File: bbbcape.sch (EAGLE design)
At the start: 13 parts

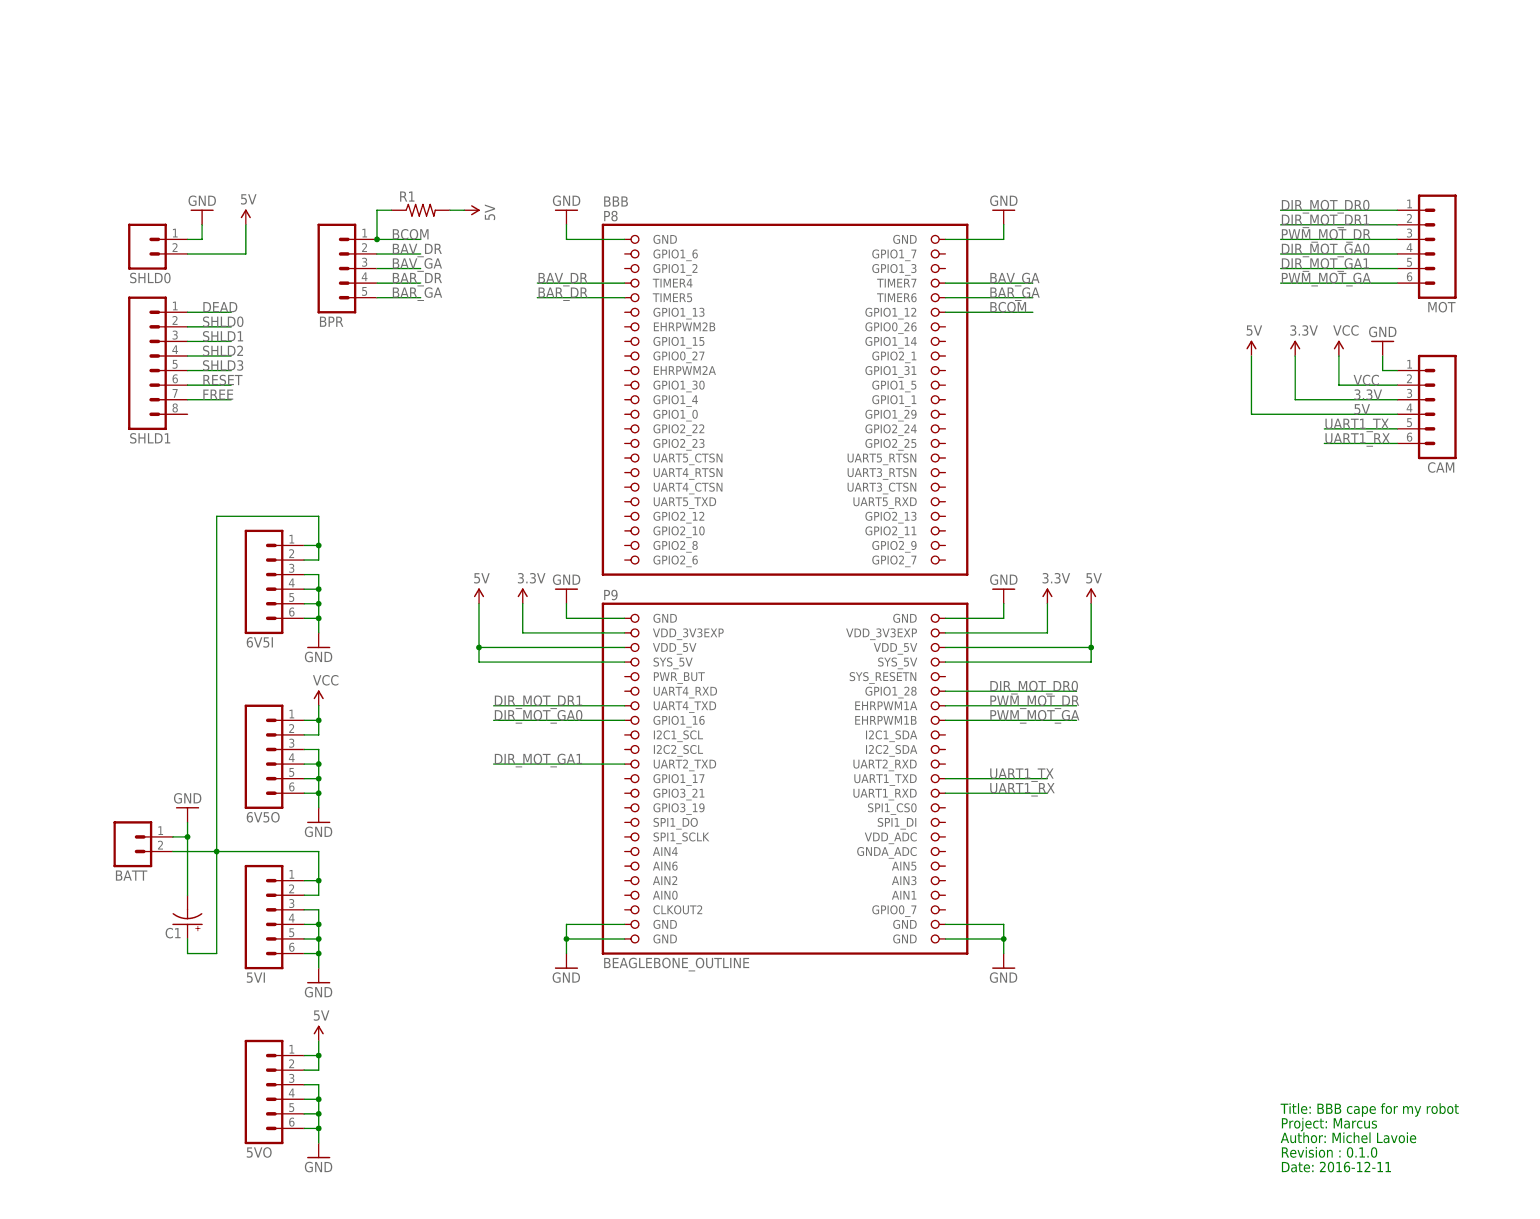
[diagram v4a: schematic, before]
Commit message: Connected GP2D12 rangefinders.
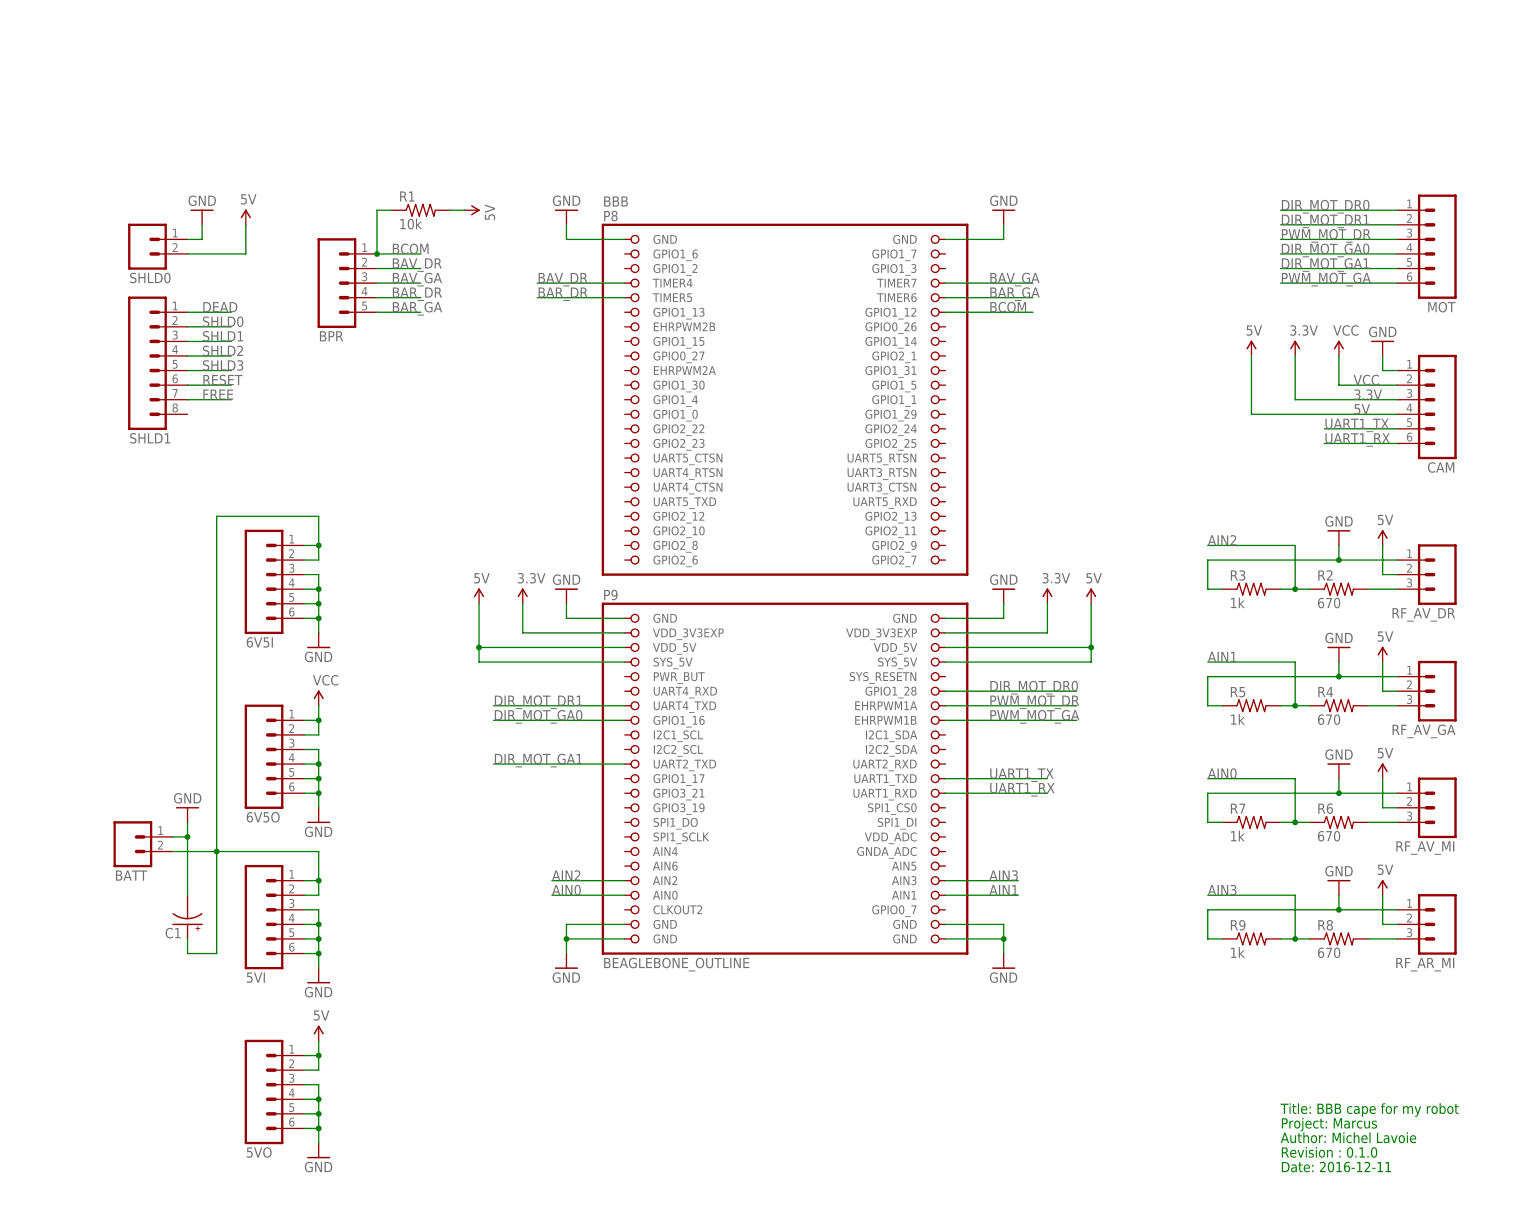
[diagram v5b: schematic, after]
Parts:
- added R2, R4, R6, R8: 670, SparkFun-Passives:RESISTORAXIAL-0.3
- added R3, R5, R7, R9: 1k, SparkFun-Passives:RESISTORAXIAL-0.3
- added RF_AR_MI, RF_AV_DR, RF_AV_GA, RF_AV_MI: (no value), SparkFun-Connectors:M03PTH
- R1: value (none) -> 10k
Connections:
- new net AIN0: BBB.AIN0, R6.1, R7.2
- new net AIN1: BBB.AIN1, R4.1, R5.2
- new net AIN2: BBB.AIN2, R2.1, R3.2
- new net AIN3: BBB.AIN3, R8.1, R9.2
- new net N$2: R2.2, RF_AV_DR.3
- new net N$4: R4.2
- new net N$5: R6.2
- new net N$6: R8.2
- net 5V: now also RF_AV_DR.2
- net GND: now also R3.1, R5.1, R7.1, R9.1, RF_AV_DR.1
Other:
- moved on the sheet: BPR

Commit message: Connected shields.
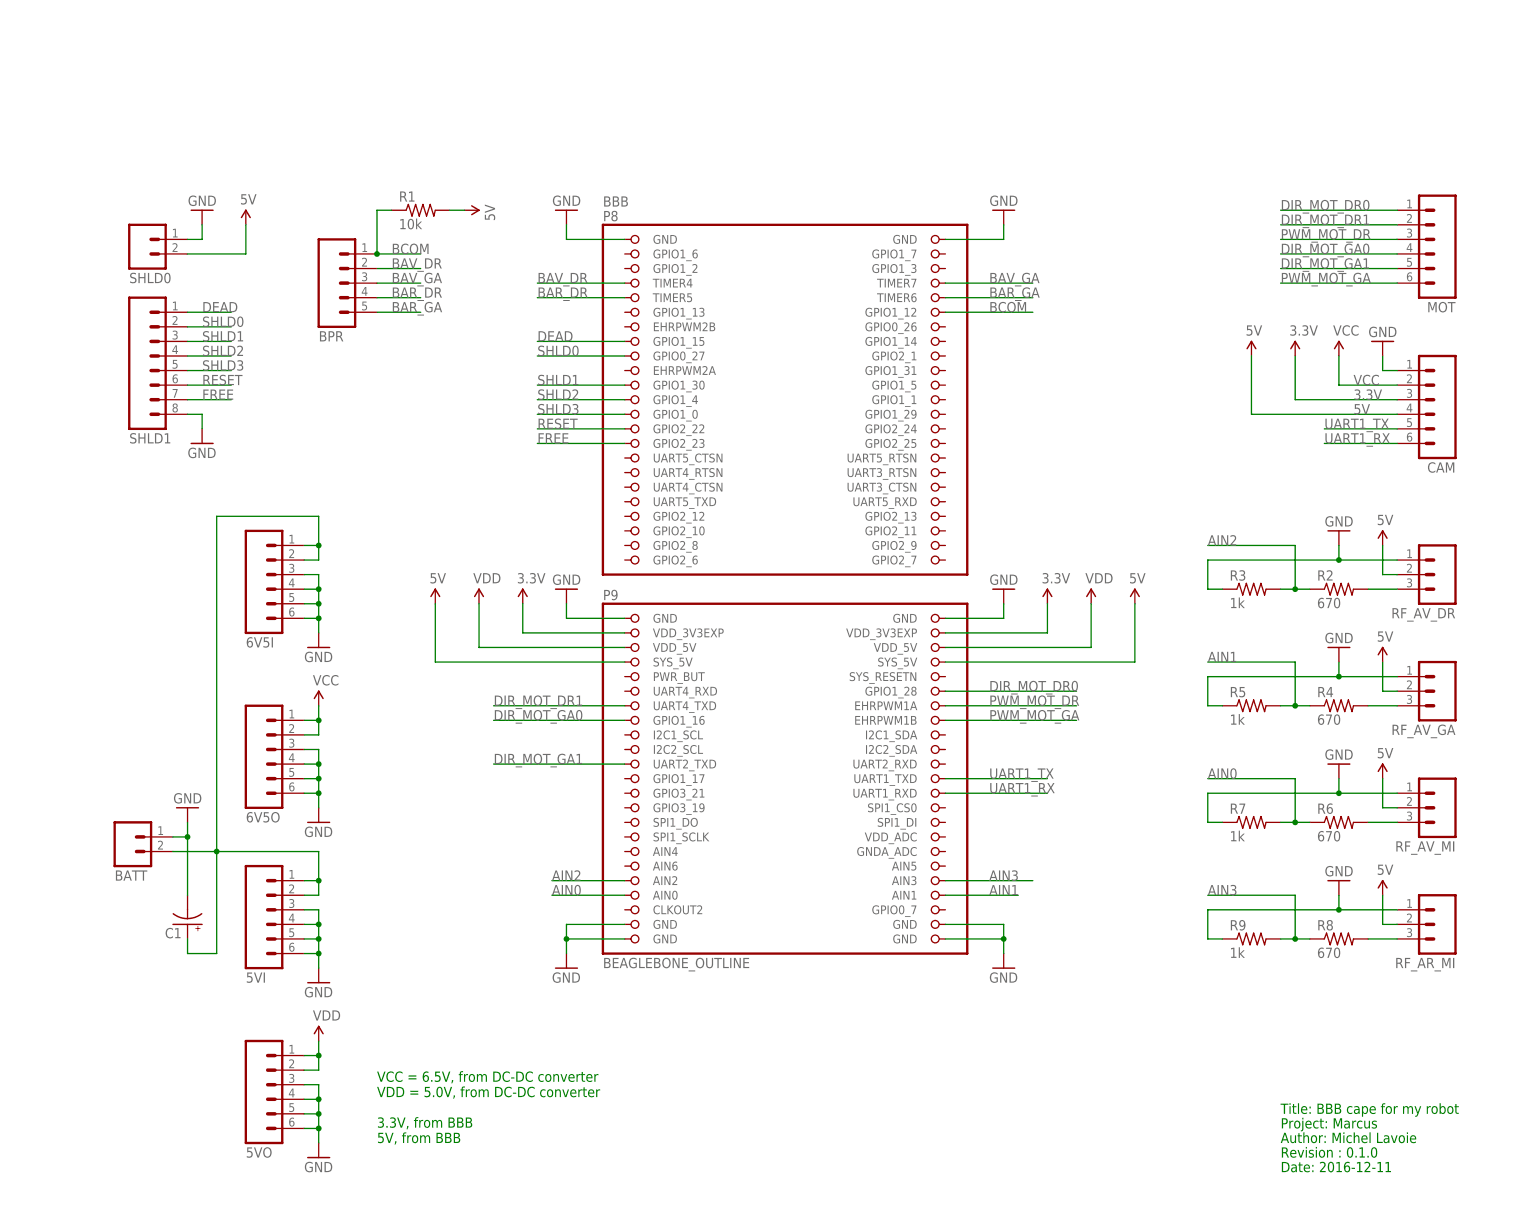
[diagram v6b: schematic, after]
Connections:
- new net VDD: 5VO.1, 5VO.2, BBB.VDD_5V@1, BBB.VDD_5V@2
- net 5V: no longer 5VO.1, 5VO.2, BBB.VDD_5V@1, BBB.VDD_5V@2
- net DEAD: now also BBB.GPIO1_15
- net FREE: now also BBB.GPIO2_23
- net GND: now also SHLD1.8
- net RESET: now also BBB.GPIO2_22
- net SHLD0: now also BBB.GPIO0_27
- net SHLD1: now also BBB.GPIO1_30
- net SHLD2: now also BBB.GPIO1_4
- net SHLD3: now also BBB.GPIO1_0
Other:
- note added: "VCC = 6.5V, from DC-DC converter VDD = 5.0V, from DC-DC converter 3.3V, from BBB 5V, from BBB"
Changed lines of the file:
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@@
 <setting verticaltext="up"/>
 </settings>
-<grid distance="0.1" unitdist="inch" unit="inch" style="lines" multiple="1" display="no" altdistance="0.01" altunitdist="inch" altunit="inch"/>
+<grid distance="0.1" unitdist="inch" unit="inch" style="dots" multiple="1" display="yes" altdistance="0.01" altunitdist="inch" altunit="inch"/>
 <layers>
 <layer number="1" name="Top" color="4" fill="1" visible="no" active="no"/>
@@
 <part name="GND6" library="SparkFun-Aesthetics" deviceset="GND" device=""/>
 <part name="GND7" library="SparkFun-Aesthetics" deviceset="GND" device=""/>
-<part name="SUPPLY1" library="SparkFun-Aesthetics" deviceset="5V" device=""/>
 <part name="BATT" library="SparkFun-Connectors" deviceset="M02" device="PTH"/>
 <part name="GND8" library="SparkFun-Aesthetics" deviceset="GND" device=""/>
@@
 <part name="GND17" library="SparkFun-Aesthetics" deviceset="GND" device=""/>
 <part name="SUPPLY13" library="SparkFun-Aesthetics" deviceset="5V" device=""/>
+<part name="SUPPLY14" library="SparkFun-Aesthetics" deviceset="VDD" device=""/>
+<part name="SUPPLY1" library="SparkFun-Aesthetics" deviceset="VDD" device=""/>
+<part name="SUPPLY15" library="SparkFun-Aesthetics" deviceset="VDD" device=""/>
+<part name="GND18" library="SparkFun-Aesthetics" deviceset="GND" device=""/>
 </parts>
 <sheets>
@@
 <text x="210.82" y="10.16" size="1.778" layer="91">Revision : 0.1.0</text>
 <text x="210.82" y="7.62" size="1.778" layer="91">Date: 2016-12-11</text>
+<text x="53.34" y="12.7" size="1.778" layer="91">VCC = 6.5V, from DC-DC converter
+VDD = 5.0V, from DC-DC converter
+3.3V, from BBB
+5V, from BBB</text>
 </plain>
 <instances>
@@
 <instance part="GND6" gate="1" x="86.36" y="43.18"/>
 <instance part="GND7" gate="1" x="162.56" y="43.18"/>
-<instance part="SUPPLY1" gate="G$1" x="43.18" y="30.48"/>
 <instance part="BATT" gate="G$1" x="10.16" y="66.04" rot="MR180"/>
 <instance part="GND8" gate="1" x="20.32" y="71.12" rot="R180"/>
@@
 <instance part="R1" gate="G$1" x="60.96" y="175.26"/>
 <instance part="SUPPLY3" gate="G$1" x="68.58" y="175.26" rot="R270"/>
-<instance part="SUPPLY4" gate="G$1" x="71.12" y="106.68"/>
-<instance part="SUPPLY5" gate="G$1" x="177.8" y="106.68"/>
+<instance part="SUPPLY4" gate="G$1" x="63.5" y="106.68"/>
+<instance part="SUPPLY5" gate="G$1" x="185.42" y="106.68"/>
 <instance part="SUPPLY6" gate="G$1" x="78.74" y="106.68"/>
 <instance part="SUPPLY7" gate="G$1" x="170.18" y="106.68"/>
@@
 <instance part="GND17" gate="1" x="220.98" y="58.42" rot="R180"/>
 <instance part="SUPPLY13" gate="G$1" x="228.6" y="55.88"/>
+<instance part="SUPPLY14" gate="VDD" x="71.12" y="106.68"/>
+<instance part="SUPPLY1" gate="VDD" x="43.18" y="30.48"/>
+<instance part="SUPPLY15" gate="VDD" x="177.8" y="106.68"/>
+<instance part="GND18" gate="1" x="22.86" y="134.62"/>
 </instances>
 <busses>
@@
 <wire x1="220.98" y1="53.34" x2="231.14" y2="53.34" width="0.1524" layer="91"/>
 <junction x="220.98" y="53.34"/>
+</segment>
+<segment>
+<pinref part="SHLD1" gate="G$1" pin="8"/>
+<wire x1="20.32" y1="139.7" x2="22.86" y2="139.7" width="0.1524" layer="91"/>
+<pinref part="GND18" gate="1" pin="GND"/>
+<wire x1="22.86" y1="139.7" x2="22.86" y2="137.16" width="0.1524" layer="91"/>
 </segment>
 </net>
@@
 <net name="5V" class="0">
 <segment>
-<pinref part="5VO" gate="G$1" pin="1"/>
-<pinref part="SUPPLY1" gate="G$1" pin="5V"/>
-<wire x1="40.64" y1="27.94" x2="43.18" y2="27.94" width="0.1524" layer="91"/>
-<wire x1="43.18" y1="27.94" x2="43.18" y2="30.48" width="0.1524" layer="91"/>
-<pinref part="5VO" gate="G$1" pin="2"/>
-<wire x1="40.64" y1="25.4" x2="43.18" y2="25.4" width="0.1524" layer="91"/>
-<wire x1="43.18" y1="25.4" x2="43.18" y2="27.94" width="0.1524" layer="91"/>
-<junction x="43.18" y="27.94"/>
-</segment>
-<segment>
 <pinref part="SHLD0" gate="G$1" pin="2"/>
 <wire x1="20.32" y1="167.64" x2="30.48" y2="167.64" width="0.1524" layer="91"/>
@@
 <segment>
 <pinref part="SUPPLY4" gate="G$1" pin="5V"/>
-<wire x1="71.12" y1="106.68" x2="71.12" y2="99.06" width="0.1524" layer="91"/>
-<pinref part="BBB" gate="G$1" pin="VDD_5V@1"/>
-<wire x1="71.12" y1="99.06" x2="96.52" y2="99.06" width="0.1524" layer="91"/>
+<wire x1="63.5" y1="106.68" x2="63.5" y2="96.52" width="0.1524" layer="91"/>
 <pinref part="BBB" gate="G$1" pin="SYS_5V@1"/>
-<wire x1="96.52" y1="96.52" x2="71.12" y2="96.52" width="0.1524" layer="91"/>
-<wire x1="71.12" y1="96.52" x2="71.12" y2="99.06" width="0.1524" layer="91"/>
-<junction x="71.12" y="99.06"/>
-</segment>
-<segment>
-<pinref part="BBB" gate="G$1" pin="VDD_5V@2"/>
-<wire x1="152.4" y1="99.06" x2="177.8" y2="99.06" width="0.1524" layer="91"/>
+<wire x1="96.52" y1="96.52" x2="63.5" y2="96.52" width="0.1524" layer="91"/>
+</segment>
+<segment>
 <pinref part="SUPPLY5" gate="G$1" pin="5V"/>
-<wire x1="177.8" y1="99.06" x2="177.8" y2="106.68" width="0.1524" layer="91"/>
+<wire x1="185.42" y1="96.52" x2="185.42" y2="106.68" width="0.1524" layer="91"/>
 <pinref part="BBB" gate="G$1" pin="SYS_5V@2"/>
-<wire x1="152.4" y1="96.52" x2="177.8" y2="96.52" width="0.1524" layer="91"/>
-<wire x1="177.8" y1="96.52" x2="177.8" y2="99.06" width="0.1524" layer="91"/>
-<junction x="177.8" y="99.06"/>
+<wire x1="152.4" y1="96.52" x2="185.42" y2="96.52" width="0.1524" layer="91"/>
 </segment>
 <segment>
@@
 <label x="22.86" y="157.48" size="1.778" layer="95"/>
 </segment>
+<segment>
+<pinref part="BBB" gate="G$1" pin="GPIO1_15"/>
+<wire x1="81.28" y1="152.4" x2="96.52" y2="152.4" width="0.1524" layer="91"/>
+<label x="81.28" y="152.4" size="1.778" layer="95"/>
+</segment>
 </net>
 <net name="SHLD0" class="0">
@@
 <label x="22.86" y="154.94" size="1.778" layer="95"/>
 </segment>
+<segment>
+<pinref part="BBB" gate="G$1" pin="GPIO0_27"/>
+<wire x1="81.28" y1="149.86" x2="96.52" y2="149.86" width="0.1524" layer="91"/>
+<label x="81.28" y="149.86" size="1.778" layer="95"/>
+</segment>
 </net>
 <net name="SHLD1" class="0">
@@
 <label x="22.86" y="152.4" size="1.778" layer="95"/>
 </segment>
+<segment>
+<pinref part="BBB" gate="G$1" pin="GPIO1_30"/>
+<wire x1="81.28" y1="144.78" x2="96.52" y2="144.78" width="0.1524" layer="91"/>
+<label x="81.28" y="144.78" size="1.778" layer="95"/>
+</segment>
 </net>
 <net name="SHLD2" class="0">
@@
 <label x="22.86" y="149.86" size="1.778" layer="95"/>
 </segment>
+<segment>
+<pinref part="BBB" gate="G$1" pin="GPIO1_4"/>
+<wire x1="81.28" y1="142.24" x2="96.52" y2="142.24" width="0.1524" layer="91"/>
+<label x="81.28" y="142.24" size="1.778" layer="95"/>
+</segment>
 </net>
 <net name="SHLD3" class="0">
@@
 <label x="22.86" y="147.32" size="1.778" layer="95"/>
 </segment>
+<segment>
+<pinref part="BBB" gate="G$1" pin="GPIO1_0"/>
+<wire x1="81.28" y1="139.7" x2="96.52" y2="139.7" width="0.1524" layer="91"/>
+<label x="81.28" y="139.7" size="1.778" layer="95"/>
+</segment>
 </net>
 <net name="RESET" class="0">
@@
 <label x="22.86" y="144.78" size="1.778" layer="95"/>
 </segment>
+<segment>
+<pinref part="BBB" gate="G$1" pin="GPIO2_22"/>
+<wire x1="81.28" y1="137.16" x2="96.52" y2="137.16" width="0.1524" layer="91"/>
+<label x="81.28" y="137.16" size="1.778" layer="95"/>
+</segment>
 </net>
 <net name="FREE" class="0">
@@
 <wire x1="27.94" y1="142.24" x2="20.32" y2="142.24" width="0.1524" layer="91"/>
 <label x="22.86" y="142.24" size="1.778" layer="95"/>
+</segment>
+<segment>
+<pinref part="BBB" gate="G$1" pin="GPIO2_23"/>
+<wire x1="81.28" y1="134.62" x2="96.52" y2="134.62" width="0.1524" layer="91"/>
+<label x="81.28" y="134.62" size="1.778" layer="95"/>
 </segment>
 </net>
@@
 <segment>
 <pinref part="BBB" gate="G$1" pin="AIN3"/>
-<wire x1="165.1" y1="58.42" x2="152.4" y2="58.42" width="0.1524" layer="91"/>
+<wire x1="167.64" y1="58.42" x2="152.4" y2="58.42" width="0.1524" layer="91"/>
 <label x="160.02" y="58.42" size="1.778" layer="95"/>
 </segment>
@@
 </segment>
 </net>
+<net name="VDD" class="0">
+<segment>
+<pinref part="SUPPLY14" gate="VDD" pin="VDD"/>
+<wire x1="71.12" y1="106.68" x2="71.12" y2="99.06" width="0.1524" layer="91"/>
+<pinref part="BBB" gate="G$1" pin="VDD_5V@1"/>
+<wire x1="71.12" y1="99.06" x2="96.52" y2="99.06" width="0.1524" layer="91"/>
+</segment>
+<segment>
+<pinref part="5VO" gate="G$1" pin="1"/>
+<wire x1="40.64" y1="27.94" x2="43.18" y2="27.94" width="0.1524" layer="91"/>
+<pinref part="SUPPLY1" gate="VDD" pin="VDD"/>
+<wire x1="43.18" y1="27.94" x2="43.18" y2="30.48" width="0.1524" layer="91"/>
+<pinref part="5VO" gate="G$1" pin="2"/>
+<wire x1="40.64" y1="25.4" x2="43.18" y2="25.4" width="0.1524" layer="91"/>
+<wire x1="43.18" y1="25.4" x2="43.18" y2="27.94" width="0.1524" layer="91"/>
+<junction x="43.18" y="27.94"/>
+</segment>
+<segment>
+<pinref part="BBB" gate="G$1" pin="VDD_5V@2"/>
+<wire x1="152.4" y1="99.06" x2="177.8" y2="99.06" width="0.1524" layer="91"/>
+<pinref part="SUPPLY15" gate="VDD" pin="VDD"/>
+<wire x1="177.8" y1="99.06" x2="177.8" y2="106.68" width="0.1524" layer="91"/>
+</segment>
+</net>
 </nets>
 </sheet>
@@
 </schematic>
 </drawing>
+<compatibility>
+<note version="6.3" minversion="6.2.2" severity="warning">
+Since Version 6.2.2 text objects can contain more than one line,
+which will not be processed correctly with this version.
+</note>
+</compatibility>
 </eagle>
